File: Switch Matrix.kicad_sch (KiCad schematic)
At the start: 216 parts

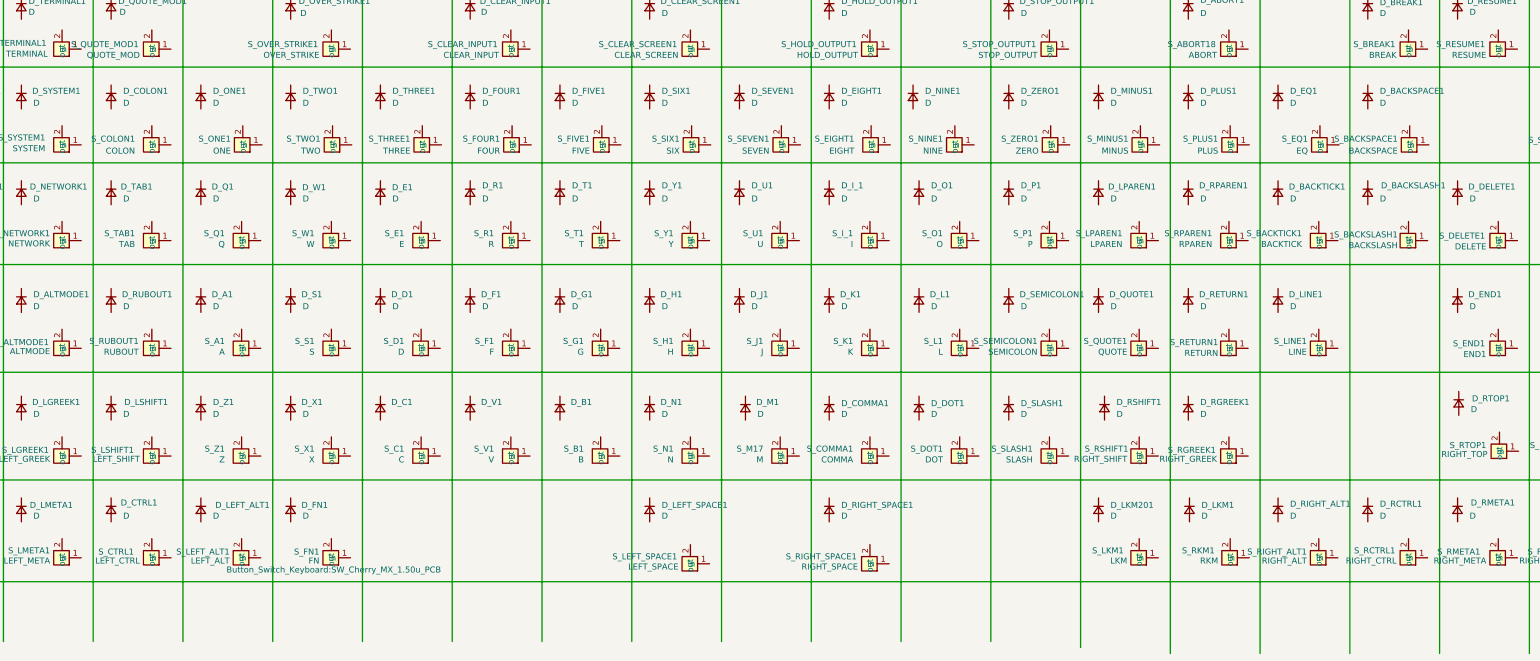
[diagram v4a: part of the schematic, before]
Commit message: fixes: bottom line and backspace, keyboard-layout.json added (keyboard-layout-editor.com)
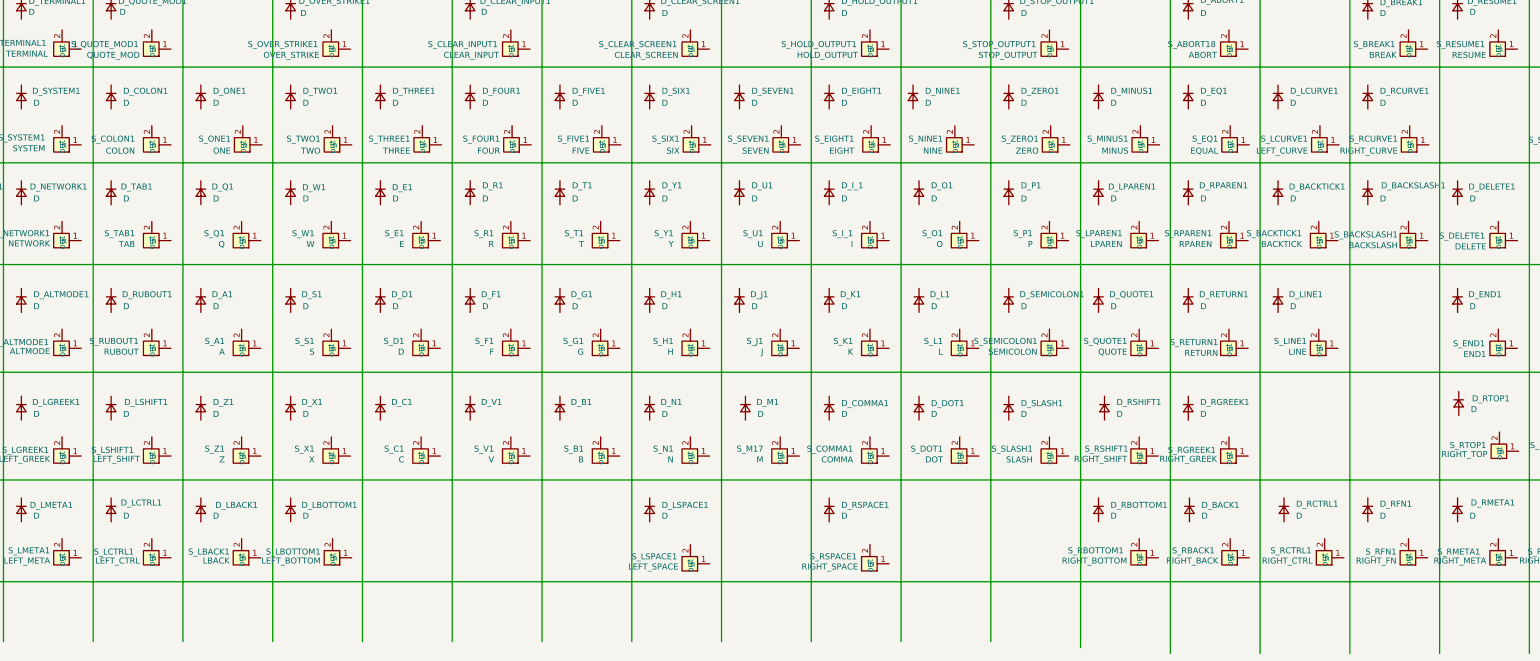
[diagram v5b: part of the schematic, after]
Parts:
- removed S_FN1: FN, Button_Switch_Keyboard:SW_Cherry_MX_1.50u_PCB, symbol Space_Cadet_Button_Switches:SWK
- added S_LBOTTOM1: LEFT_BOTTOM, Button_Switch_Keyboard:SW_Cherry_MX_1.25u_PCB, symbol Space_Cadet_Button_Switches:SWK
- S_EQ1: renamed from S_PLUS1; value PLUS -> EQUAL; footprint Button_Switch_Keyboard:SW_Cherry_MX_1.00u_PCB -> Button_Switch_Keyboard:SW_Cherry_MX_1.50u_PCB
- S_LBACK1: renamed from S_LEFT_ALT1; value LEFT_ALT -> LBACK; footprint Button_Switch_Keyboard:SW_Cherry_MX_1.50u_PCB -> Button_Switch_Keyboard:SW_Cherry_MX_1.25u_PCB; dep S_CTRL1 -> S_LCTRL1
- S_LCTRL1: renamed from S_CTRL1; footprint Button_Switch_Keyboard:SW_Cherry_MX_1.50u_PCB -> Button_Switch_Keyboard:SW_Cherry_MX_1.75u_PCB
- S_LCURVE1: renamed from S_EQ1; value EQ -> LEFT_CURVE; dep S_PLUS1 -> S_EQ1
- S_LSPACE1: renamed from S_LEFT_SPACE1; dep S_FN1 -> S_LBOTTOM1
- S_MINUS1: footprint Button_Switch_Keyboard:SW_Cherry_MX_1.00u_PCB -> Button_Switch_Keyboard:SW_Cherry_MX_1.50u_PCB
- S_RBACK1: renamed from S_RKM1; value RKM -> RIGHT_BACK; dep S_LKM1 -> S_RBOTTOM1
- S_RBOTTOM1: renamed from S_LKM1; value LKM -> RIGHT_BOTTOM; dep S_RIGHT_SPACE1 -> S_RSPACE1
- S_RCTRL1: footprint Button_Switch_Keyboard:SW_Cherry_MX_1.50u_PCB -> Button_Switch_Keyboard:SW_Cherry_MX_1.75u_PCB; dep S_RIGHT_ALT1 -> S_RBACK1
- S_RCURVE1: renamed from S_BACKSPACE1; value BACKSPACE -> RIGHT_CURVE; footprint Button_Switch_Keyboard:SW_Cherry_MX_2.00u_PCB -> Button_Switch_Keyboard:SW_Cherry_MX_1.00u_PCB; dep S_EQ1 -> S_LCURVE1
- S_RFN1: renamed from S_RIGHT_ALT1; value RIGHT_ALT -> RIGHT_FN; dep S_RKM1 -> S_RCTRL1
- S_RMETA1: dep S_RCTRL1 -> S_RFN1
- S_RSPACE1: renamed from S_RIGHT_SPACE1; dep S_LEFT_SPACE1 -> S_LSPACE1
- S_STATUS1: dep S_BACKSPACE1 -> S_RCURVE1
- renumbered D_LKM1 to D_BACK1, D_PLUS1 to D_EQ1, D_LEFT_ALT1 to D_LBACK1, D_FN1 to D_LBOTTOM1, D_CTRL1 to D_LCTRL1, D_EQ1 to D_LCURVE1, D_LEFT_SPACE1 to D_LSPACE1, D_LKM201 to D_RBOTTOM1, D_BACKSPACE1 to D_RCURVE1, D_RIGHT_ALT1 to D_RFN1, D_RIGHT_SPACE1 to D_RSPACE1
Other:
- moved on the sheet: D_RCTRL1, D_RFN1, S_RCTRL1, S_RFN1

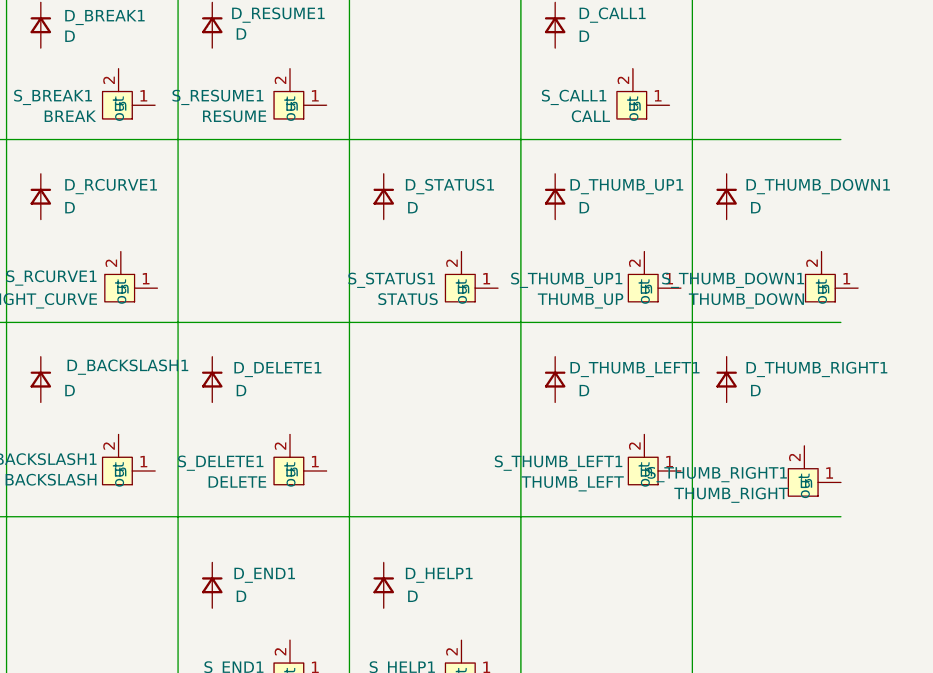
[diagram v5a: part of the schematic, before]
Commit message: wip: gerber layear is B_Fab now, descrease size to A4
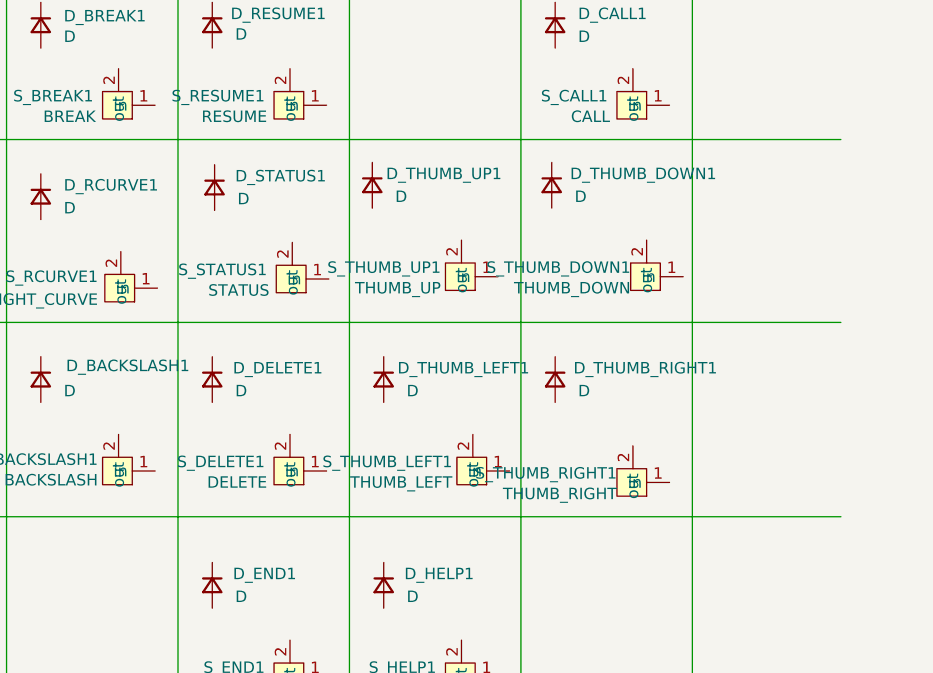
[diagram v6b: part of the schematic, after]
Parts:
- D_A1, D_ABORT1, D_ALTLOCK1, D_ALTMODE1, D_B1, D_BACK1, D_BACKSLASH1, D_BACKTICK1, D_BREAK1, D_C1, D_CALL1, D_CAPS_LOCK1, D_CLEAR_INPUT1, D_CLEAR_SCREEN1, D_COLON1, D_COMMA1, D_D1, D_DELETE1, D_DOT1, D_E1, D_EIGHT1, D_END1, D_EQ1, D_F1, D_FIVE1, D_FOUR1, D_G1, D_H1, D_HELP1, D_HOLD_OUTPUT1, D_I_1, D_J1, D_K1, D_L1, D_LBACK1, D_LBOTTOM1, D_LCTRL1, D_LCURVE1, D_LGREEK1, D_LHYPER1, D_LHYPO1, D_LINE1, D_LMETA1, D_LPAREN1, D_LSHIFT1, D_LSPACE1, D_LSUPER1, D_LTOP1, D_M1, D_MACRO1, D_MINUS1, D_MODE_LOCK1, D_N1, D_NETWORK1, D_NINE1, D_O1, D_ONE1, D_OVER_STRIKE1, D_P1, D_Q1, D_QUOTE1, D_QUOTE_MOD1, D_R1, D_RBOTTOM1, D_RCTRL1, D_RCURVE1, D_REPEAT1, D_RESUME1, D_RETURN1, D_RFN1, D_RGREEK1, D_RHYPER1, D_RHYPO1, D_RMETA1, D_ROM_FOUR1, D_ROM_ONE1, D_ROM_THREE1, D_ROM_TWO1, D_RPAREN1, D_RSHIFT1, D_RSPACE1, D_RSUPER1, D_RTOP1, D_RUBOUT1, D_S1, D_SEMICOLON1, D_SEVEN1, D_SIX1, D_SLASH1, D_STATUS1, D_STOP_OUTPUT1, D_SYSTEM1, D_T1, D_TAB1, D_TERMINAL1, D_THREE1, D_THUMB_DOWN1, D_THUMB_LEFT1, D_THUMB_RIGHT1, D_THUMB_UP1, D_TWO1, D_U1, D_V1, D_W1, D_X1, D_Y1, D_Z1, D_ZERO1: footprint Diode_SMD:D_SOD-123 -> Diode_THT:D_DO-41_SOD81_P7.62mm_Horizontal
- S_RGREEK1: footprint Button_Switch_Keyboard:SW_Cherry_MX_1.50u_Plate -> Button_Switch_Keyboard:SW_Cherry_MX_1.50u_PCB
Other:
- moved on the sheet: D_STATUS1, D_THUMB_DOWN1, D_THUMB_LEFT1, D_THUMB_RIGHT1, D_THUMB_UP1, S_STATUS1, S_THUMB_DOWN1, S_THUMB_LEFT1, S_THUMB_RIGHT1, S_THUMB_UP1

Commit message: wip: wiring begin
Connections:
- net COL0: now also S_CAPSLOCK1.1 (in), S_LHYPER1.1 (in), S_LHYPO1.1 (in), S_LSUPER1.1 (in), S_LTOP1.1 (in), S_MACRO1.1 (in), S_M_LOCK1.1 (in), S_ROM_FOUR1.1 (in), S_ROM_ONE1.1 (in), S_ROM_THREE1.1 (in), S_ROM_TWO1.1 (in)
- net COL3: now also S_ALTMODE1.1 (in), S_COLON1.1 (in), S_LCTRL1.1 (in), S_LGREEK1.1 (in), S_LMETA1.1 (in), S_LSHIFT1.1 (in), S_NETWORK1.1 (in), S_RUBOUT1.1 (in), S_SYSTEM1.1 (in), S_TAB1.1 (in), S_TERMINAL1.1 (in)
- net ROW0: now also D_MACRO1.1 (K), D_TERMINAL1.1 (K)
- net ROW1: now also D_ROM_ONE1.1 (K), D_SYSTEM1.1 (K)
- net ROW2: now also D_COLON1.1 (K), D_ROM_TWO1.1 (K)
- net ROW3: now also D_NETWORK1.1 (K), D_ROM_THREE1.1 (K)
- net ROW4: now also D_ROM_FOUR1.1 (K), D_TAB1.1 (K)
- net ROW5: now also D_MODE_LOCK1.1 (K), D_RUBOUT1.1 (K)
- net ROW6: now also D_ALTMODE1.1 (K)
- net at S_ROM_ONE1.2 (out): now also D_ROM_ONE1.2 (A)
- net at D_ROM_FOUR1.2 (A): now also S_ROM_FOUR1.2 (out)
- net at S_LSHIFT1.2 (out): now also D_LSHIFT1.2 (A)
- net ROW9: now reaches D_LHYPER1.1 (K)
- net ROW9: now also D_LMETA1.1 (K)
- net at D_LHYPER1.2 (A): now also S_LHYPER1.2 (out)
- net at S_ROM_THREE1.2 (out): now also D_ROM_THREE1.2 (A)
- net at D_TAB1.2 (A): now also S_TAB1.2 (out)
- net at S_LSUPER1.2 (out): now also D_LSUPER1.2 (A)
- net at D_MODE_LOCK1.2 (A): now also S_M_LOCK1.2 (out)
- net at D_COLON1.2 (A): now also S_COLON1.2 (out)
- net at D_ROM_TWO1.2 (A): now also S_ROM_TWO1.2 (out)
- net at S_LHYPO1.2 (out): now also D_LHYPO1.2 (A)
- net ROW10: now reaches D_LCTRL1.1 (K)
- net ROW10: now also D_LHYPO1.1 (K), D_LSUPER1.1 (K)
- net at D_LCTRL1.2 (A): now also S_LCTRL1.2 (out)
- net ROW8: now reaches D_LSHIFT1.1 (K)
- net ROW8: now also D_LTOP1.1 (K)
- net ROW7: now reaches D_CAPS_LOCK1.1 (K)
- net ROW7: now also D_LGREEK1.1 (K)
- net at D_CAPS_LOCK1.2 (A): now also S_CAPSLOCK1.2 (out)
- net at S_LTOP1.2 (out): now also D_LTOP1.2 (A)
- net at D_LGREEK1.2 (A): now also S_LGREEK1.2 (out)
- net at S_NETWORK1.2 (out): now also D_NETWORK1.2 (A)
- net at S_MACRO1.2 (out): now also D_MACRO1.2 (A)
- net at D_QUOTE_MOD1.2 (A): now also S_QUOTE_MOD1.2 (out)
- net at D_SYSTEM1.2 (A): now also S_SYSTEM1.2 (out)
- net at S_LMETA1.2 (out): now also D_LMETA1.2 (A)
- net at S_TERMINAL1.2 (out): now also D_TERMINAL1.2 (A)
- net at S_RUBOUT1.2 (out): now also D_RUBOUT1.2 (A)
- net at D_ALTMODE1.2 (A): now also S_ALTMODE1.2 (out)
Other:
- moved on the sheet: D_MACRO1, D_ROM_ONE1

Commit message: wip: continue wiring
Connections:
- net COL1: now also S_ALTMODE1.1 (in), S_COLON1.1 (in), S_LCTRL1.1 (in), S_LGREEK1.1 (in), S_LMETA1.1 (in), S_LSHIFT1.1 (in), S_NETWORK1.1 (in), S_RUBOUT1.1 (in), S_SYSTEM1.1 (in), S_TAB1.1 (in), S_TERMINAL1.1 (in)
- net COL3: now also S_C1.1 (in), S_D1.1 (in), S_E1.1 (in), S_F1.1 (in), S_FOUR1.1 (in), S_LSPACE1.1 (in), S_OVER_STRIKE1.1 (in), S_R1.1 (in), S_THREE1.1 (in), S_V1.1 (in); no longer S_ALTMODE1.1 (in), S_COLON1.1 (in), S_LCTRL1.1 (in), S_LGREEK1.1 (in), S_LMETA1.1 (in), S_LSHIFT1.1 (in), S_NETWORK1.1 (in), S_RUBOUT1.1 (in), S_SYSTEM1.1 (in), S_TAB1.1 (in), S_TERMINAL1.1 (in)
- net COL9: now also S_B1.1 (in), S_CLEAR_INPUT1.1 (in), S_FIVE1.1 (in), S_G1.1 (in), S_T1.1 (in)
- net ROW0: now also D_CLEAR_INPUT1.1 (K), D_OVER_STRIKE1.1 (K), D_QUOTE_MOD1.1 (K)
- net ROW1: now also D_FIVE1.1 (K), D_ONE1.1 (K), D_THREE1.1 (K)
- net ROW10: now also D_LBOTTOM1.1 (K)
- net ROW2: now also D_FOUR1.1 (K), D_TWO1.1 (K)
- net ROW3: now also D_E1.1 (K), D_Q1.1 (K), D_T1.1 (K)
- net ROW4: now also D_R1.1 (K), D_W1.1 (K)
- net ROW5: now also D_F1.1 (K), D_S1.1 (K)
- net ROW6: now also D_A1.1 (K), D_D1.1 (K), D_G1.1 (K)
- net ROW7: now also D_B1.1 (K), D_C1.1 (K), D_Z1.1 (K)
- net ROW8: now also D_N1.1 (K), D_V1.1 (K), D_X1.1 (K)
- net ROW9: now also D_LBACK1.1 (K), D_LSPACE1.1 (K)
- net at S_G1.2 (out): now also D_G1.2 (A)
- net at D_FOUR1.2 (A): now also S_FOUR1.2 (out)
- net at D_LSPACE1.2 (A): now also S_LSPACE1.2 (out)
- net at D_THREE1.2 (A): now also S_THREE1.2 (out)
- net COL2: now reaches S_S1.1 (in)
- net COL2: now also S_A1.1 (in), S_LBACK1.1 (in), S_LBOTTOM1.1 (in), S_ONE1.1 (in), S_Q1.1 (in), S_QUOTE_MOD1.1 (in), S_TWO1.1 (in), S_W1.1 (in), S_X1.1 (in), S_Z1.1 (in)
- net at S_S1.2 (out): now also D_S1.2 (A)
- net at D_D1.2 (A): now also S_D1.2 (out)
- net at S_T1.2 (out): now also D_T1.2 (A)
- net at D_A1.2 (A): now also S_A1.2 (out)
- net at D_E1.2 (A): now also S_E1.2 (out)
- net at D_Q1.2 (A): now also S_Q1.2 (out)
- net at D_W1.2 (A): now also S_W1.2 (out)
- net at D_LBOTTOM1.2 (A): now also S_LBOTTOM1.2 (out)
- net at D_X1.2 (A): now also S_X1.2 (out)
- net at S_FIVE1.2 (out): now also D_FIVE1.2 (A)
- net at S_F1.2 (out): now also D_F1.2 (A)
- net at D_LBACK1.2 (A): now also S_LBACK1.2 (out)
- net at S_OVER_STRIKE1.2 (out): now also D_OVER_STRIKE1.2 (A)
- net at S_Z1.2 (out): now also D_Z1.2 (A)
- net at D_C1.2 (A): now also S_C1.2 (out)
- net at D_B1.2 (A): now also S_B1.2 (out)
- net at S_V1.2 (out): now also D_V1.2 (A)
- net at D_CLEAR_INPUT1.2 (A): now also S_CLEAR_INPUT1.2 (out)
- net at S_ONE1.2 (out): now also D_ONE1.2 (A)
- net at D_R1.2 (A): now also S_R1.2 (out)
- net at S_TWO1.2 (out): now also D_TWO1.2 (A)
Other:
- moved on the sheet: D_CLEAR_INPUT1, D_LSPACE1, D_OVER_STRIKE1, D_QUOTE_MOD1, D_TERMINAL1, S_CLEAR_INPUT1, S_LSPACE1, S_OVER_STRIKE1, S_QUOTE_MOD1, S_TERMINAL1
